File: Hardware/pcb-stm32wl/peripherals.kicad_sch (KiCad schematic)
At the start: 52 parts, among them J10 Qwiic, J11 Conn_02x08_Odd_Even, J13 Conn_02x08_Odd_Even, J8 DEBUG, J9 UART/I2C, Q2 PMST4401,115, SW1 USR_BTN, SW2 RESET, U10 SHTC3, U3 AD7124-8BCPZ-RL7, U6 ICM-42605, U7 MRF89XAM9AT-I/RM

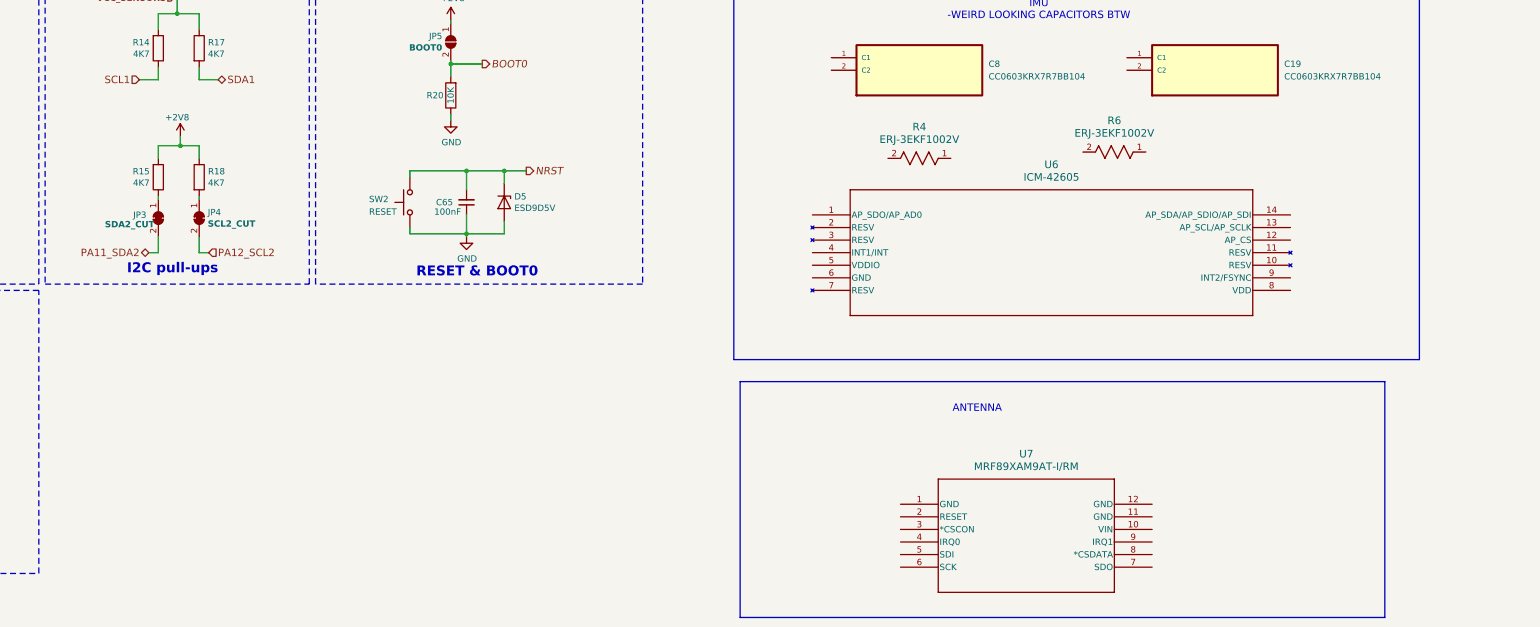
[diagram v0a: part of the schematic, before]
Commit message: wired, and selected capacitors. Not sure if they are correct as there was nothing in datasheet for it
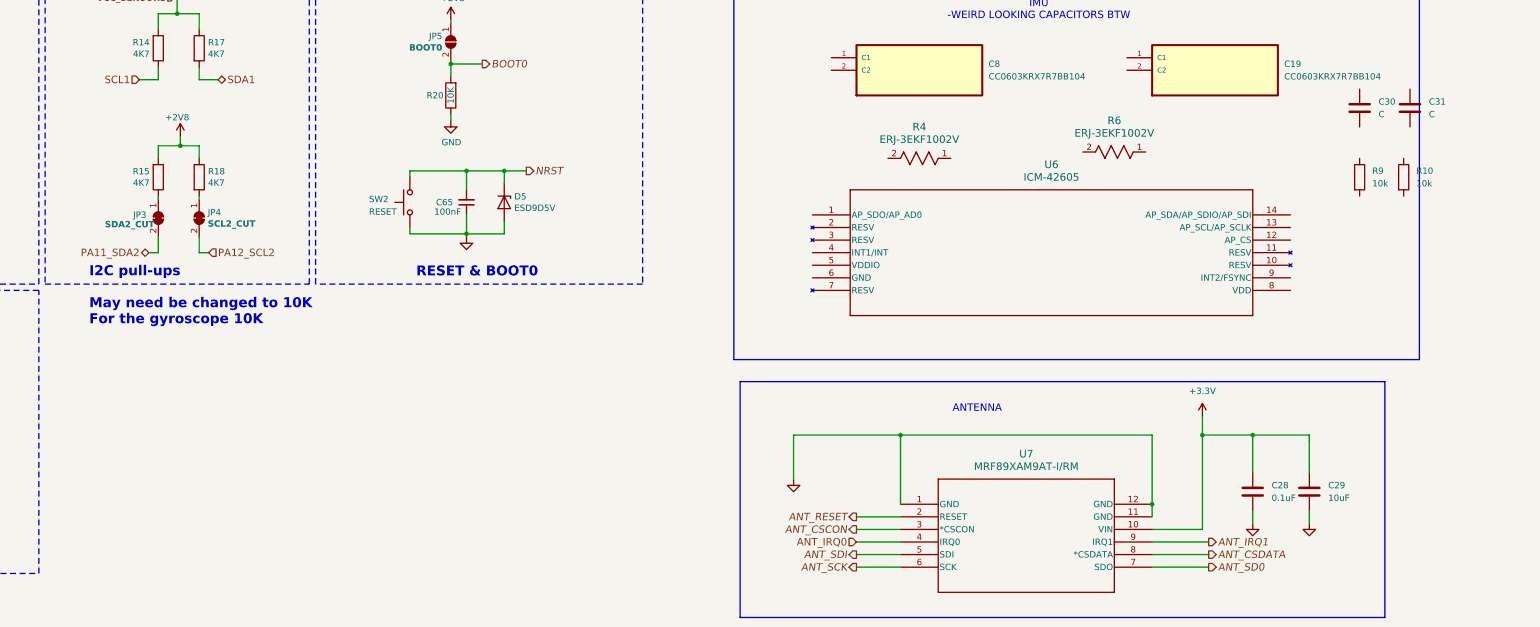
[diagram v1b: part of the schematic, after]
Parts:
- added C28: 0.1uF, symbol Device:C
- added C29: 10uF, symbol Device:C
- added C30, C31: C, symbol Device:C
- added R10, R9: 10k, symbol Device:R
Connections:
- net GND: now also U7.1 (GND), U7.11 (GND), U7.12 (GND), C28.2, C29.2
- net +3.3V: now reaches U7.10 (VIN)
- net +3.3V: now also C28.1, C29.1
- net ANT_RESET: now reaches U7.2 (RESET)
- net ANT_CSCON: now reaches U7.3 (*CSCON)
- net ANT_IRQ0: now reaches U7.4 (IRQ0)
- net ANT_SDI: now reaches U7.5 (SDI)
- net ANT_SCK: now reaches U7.6 (SCK)
- net ANT_SD0: now reaches U7.7 (SDO)
- net ANT_CSDATA: now reaches U7.8 (*CSDATA)
- net ANT_IRQ1: now reaches U7.9 (IRQ1)
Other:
- note added: "I2C pull-ups May need be changed to 10K For the gyroscope 10K"
- note removed: "I2C pull-ups"

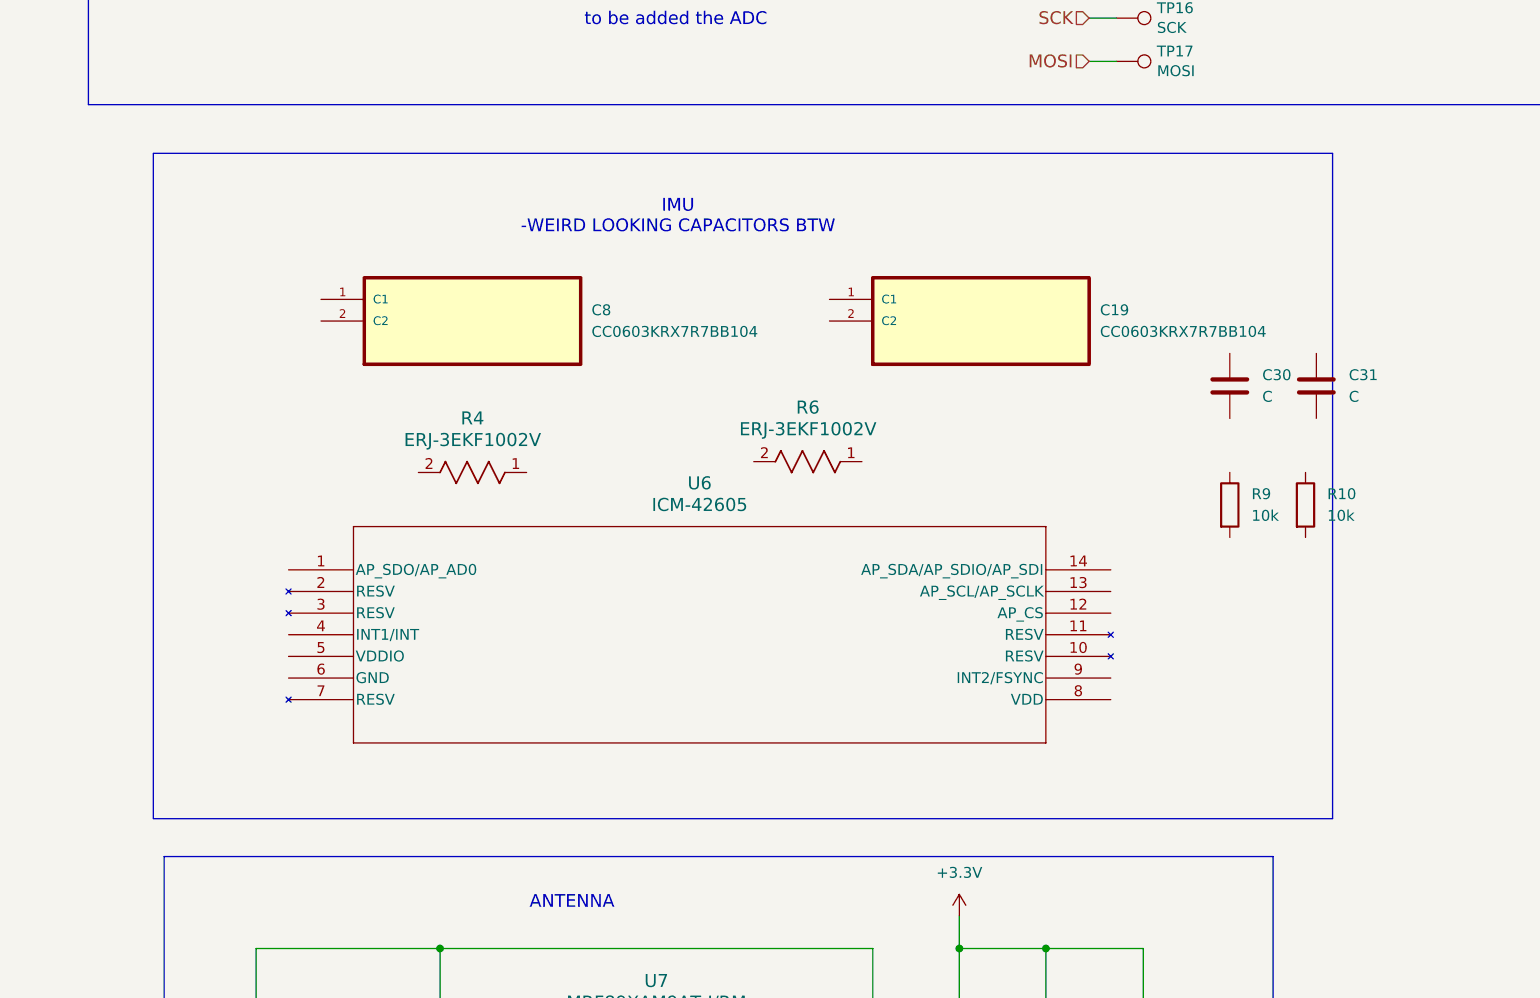
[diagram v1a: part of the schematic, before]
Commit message: gyroscope components wired and added. Pullup resistors may conflict with the other 3.3K pullup
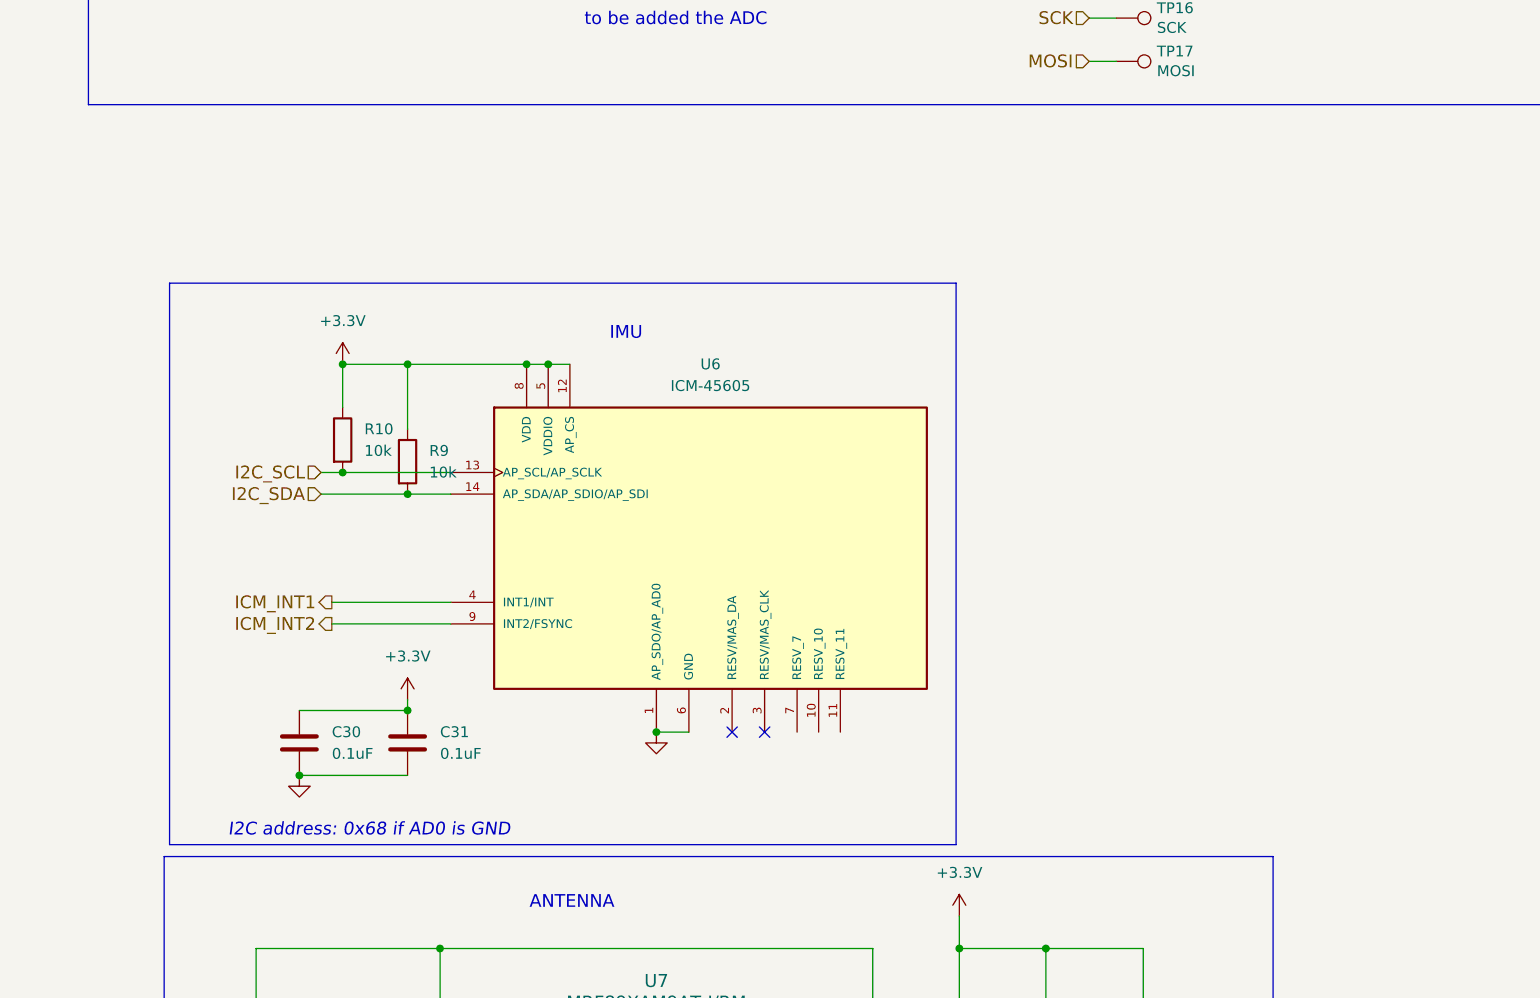
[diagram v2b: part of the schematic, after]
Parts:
- removed C19, C8: CC0603KRX7R7BB104, CC0603KRX7R7BB104:CAPC1608X90, symbol CC0603KRX7R7BB104-Gyro0.1uF:CC0603KRX7R7BB104
- removed R4, R6: ERJ-3EKF1002V, RC0603N_PAN, symbol ERJ-3EKF1002V-10k-PU:ERJ-3EKF1002V
- removed U6: ICM-42605, LGA14_2P5X3X0P91_IVS, symbol ICM-42605-gyroscope:ICM-42605
- added U6: ICM-45605, ICM-45605:XDCR_ICM-45605, symbol ICM-45605:ICM-45605
- C28: footprint (none) -> Capacitor_SMD:C_0603_1608Metric; Distributor link (none) -> https://www.digikey.ca/en/products/detail/samsung-electro-m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; MPN (none) -> CL05B104KP5NNNC; Manufacturer Part Number (none) -> CL31B106KAHNNNE; URL (none) -> https://www.digikey.ca/en/products/detail/samsung-electro-m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
- C29: footprint (none) -> Capacitor_SMD:C_1206_3216Metric; MPN (none) -> CL31B106KAHNNNE; URL (none) -> https://www.digikey.ca/en/products/detail/samsung-electro-m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
- C30, C31: value C -> 0.1uF; footprint (none) -> Capacitor_SMD:C_0603_1608Metric; Distributor link (none) -> https://www.digikey.ca/en/products/detail/samsung-electro-m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; MPN (none) -> CL05B104KP5NNNC; Manufacturer Part Number (none) -> CL31B106KAHNNNE; URL (none) -> https://www.digikey.ca/en/products/detail/samsung-electro-m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
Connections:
- net +3.3V: now also C30.1, C31.1, R10.1, R9.1, U6.12 (AP_CS), U6.5 (VDDIO), U6.8 (VDD)
- net GND: now also C30.2, C31.2, U6.1 (AP_SDO/AP_AD0), U6.6 (GND)
- net I2C_SDA: now reaches R9.2
- net I2C_SDA: now also U6.14 (AP_SDA/AP_SDIO/AP_SDI)
- net I2C_SCL: now reaches R10.2
- net I2C_SCL: now also U6.13 (AP_SCL/AP_SCLK)
- new net ICM_INT1: U6.4 (INT1/INT)
- new net ICM_INT2: U6.9 (INT2/FSYNC)
- no-connect marks 0 -> 2
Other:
- note added: "I2C address: 0x68 if AD0 is GND"
- note added: "IMU"
- note removed: "IMU -WEIRD LOOKING CAPACITORS BTW"
- moved on the sheet: C30, C31, R10, R9

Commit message: completed first attempt at wiring this horrendous adc
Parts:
- removed TP14: CS, TestPoint:TestPoint_Pad_D1.5mm, symbol Connector:TestPoint
- removed TP15: MISO, TestPoint:TestPoint_Pad_D1.5mm, symbol Connector:TestPoint
- removed TP16: SCK, TestPoint:TestPoint_Pad_D1.5mm, symbol Connector:TestPoint
- removed TP17: MOSI, TestPoint:TestPoint_Pad_D1.5mm, symbol Connector:TestPoint
- added C19, C32, C33, C8: 0.1uF, Capacitor_SMD:C_0603_1608Metric, symbol Device:C
- added C35, C36: 1uF, Capacitor_SMD:C_0402_1005Metric, symbol Device:C
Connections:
- net +2V8: no longer D3.3 (BK), JP5.1 (A), R15.2, R18.1, R19.1
- net +3.3V: now also D3.3 (BK), JP5.1 (A), R15.2, R18.1, R19.1, U3.2 (IOVDD), U3.26 (AVDD), U3.27 (*SYNC), C32.1, C33.1, C35.1, C36.1
- net AIN0: now also U3.4 (AIN0/IOUT/VBIAS)
- net AIN1: now also U3.5 (AIN1/IOUT/VBIAS)
- net AIN10: now also U3.16 (AIN10/IOUT/VBIAS)
- net AIN11: now also U3.17 (AIN11/IOUT/VBIAS)
- net AIN12: now also U3.18 (AIN12/IOUT/VBIAS)
- net AIN13: now also U3.19 (AIN13/IOUT/VBIAS)
- net AIN14: now also U3.20 (AIN14/IOUT/VBIAS/REFIN2(+))
- net AIN15: now also U3.21 (AIN15/IOUT/VBIAS/REFIN2(-))
- net AIN2: now also U3.6 (AIN2/IOUT/VBIAS/P1)
- net AIN3: now also U3.7 (AIN3/IOUT/VBIAS/P2)
- net AIN4: now also U3.8 (AIN4/IOUT/VBIAS/P3)
- net AIN5: now also U3.9 (AIN5/IOUT/VBIAS/P4)
- net AIN6: now also U3.10 (AIN6/IOUT/VBIAS)
- net AIN7: now also U3.11 (AIN7/IOUT/VBIAS)
- net AIN8: now also U3.14 (AIN8/IOUT/VBIAS)
- net AIN9: now also U3.15 (AIN9/IOUT/VBIAS)
- net GND: now also U3.23 (AVSS), U3.25 (PSW), U3.3 (DGND), C19.2, C32.2, C33.2, C35.2, C36.2, C8.2
- net MISO: now also U3.28 (DOUT/*RDY)
- net MOSI: now also U3.29 (DIN)
- net SCK: now also U3.30 (SCLK)
- net strainGaugeCS: now also U3.32 (*CS)
- net at U3.1 (REGCAPD): now also C8.1
- net at U3.24 (REGCAPA): now also C19.1
- no-connect marks 2 -> 10
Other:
- note removed: "to be added the ADC"
- moved on the sheet: D3, JP3, JP4, JP5, R15, R18, R20, R21, R22, R23, U3
